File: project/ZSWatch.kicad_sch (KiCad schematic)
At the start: 35 parts, among them IC1 nPM1300-QEXX, IC2 TS3USB221A, IC3 AT25SL128A, M1 NORA-B106, X1 DOCK, X2 INT, X3 VBAT, X4 VBUS, X5 3V3

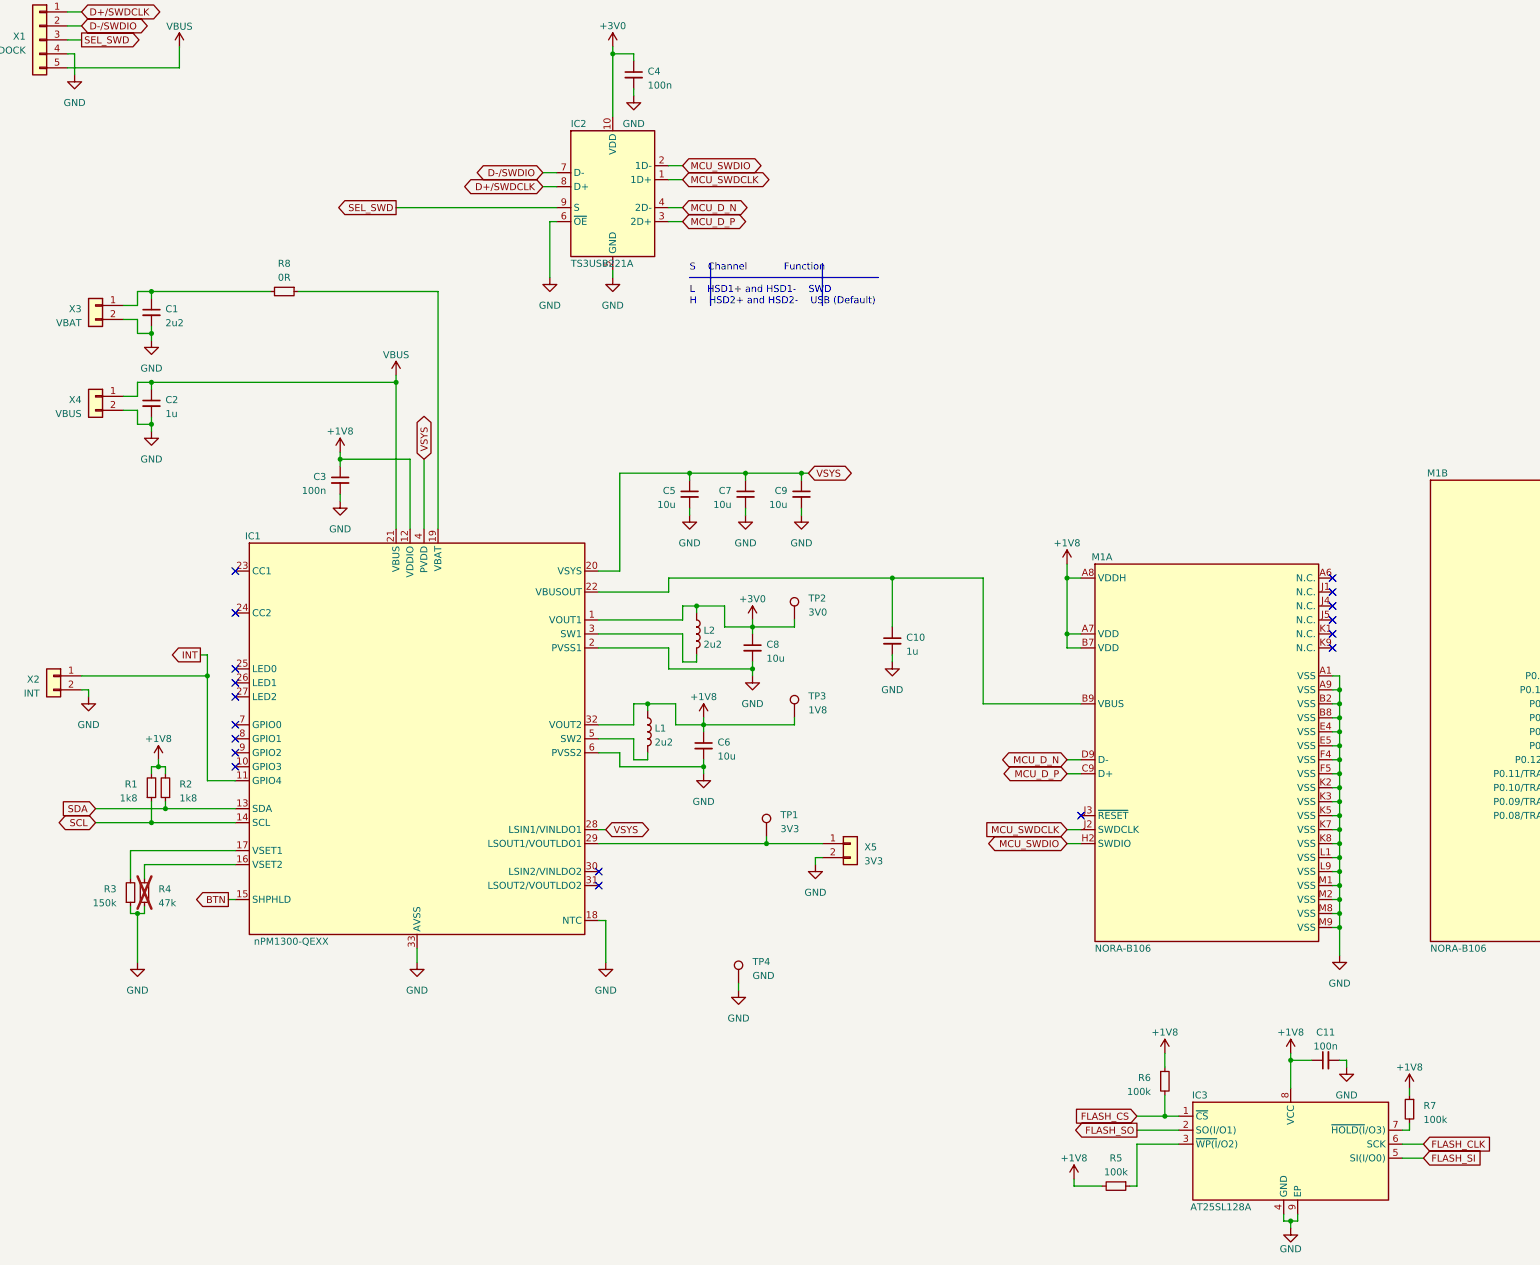
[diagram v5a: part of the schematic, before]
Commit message: Add additional jumper for SEL pin
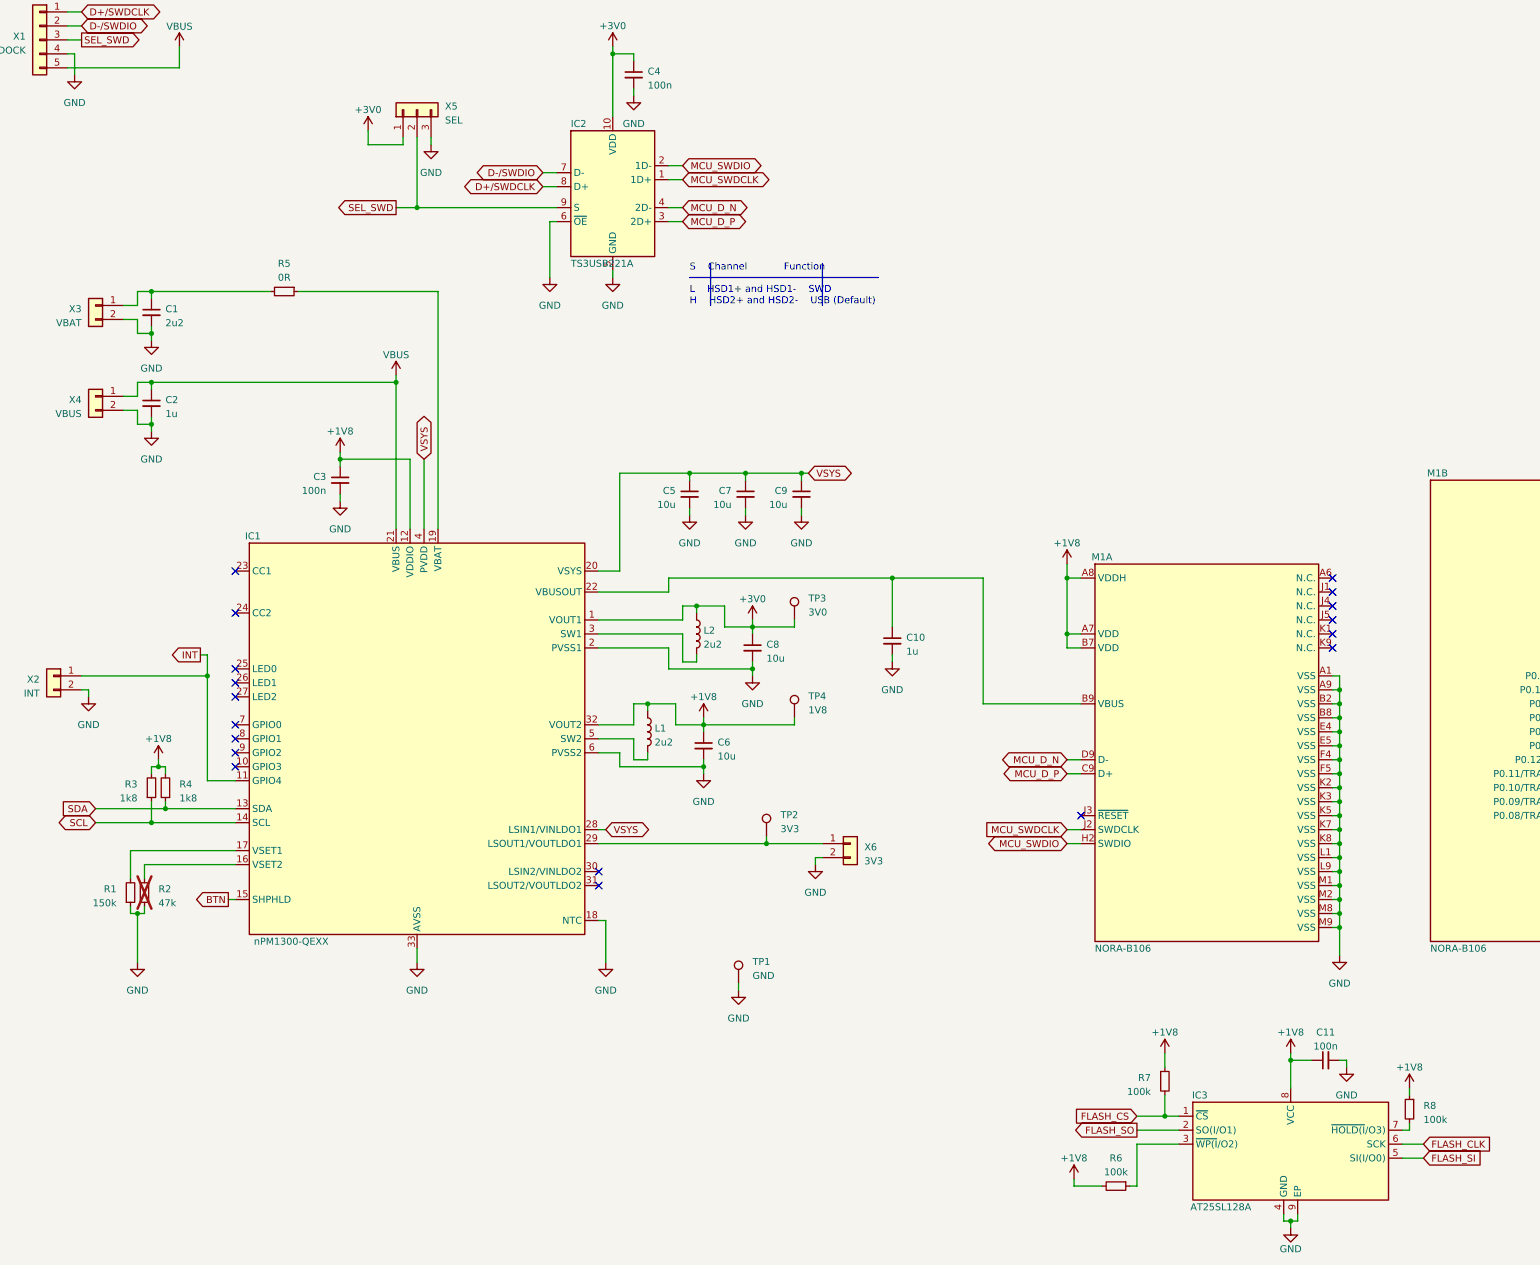
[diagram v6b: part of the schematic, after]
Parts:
- added X5: SEL, Connector_PinHeader_2.54mm:PinHeader_1x03_P2.54mm_Vertical, symbol Connector_Generic:Conn_01x03
- renumbered R3 to R1, R4 to R2, R1 to R3, R2 to R4, R8 to R5, R5 to R6, R6 to R7, R7 to R8, TP4 to TP1, TP1 to TP2, TP2 to TP3, TP3 to TP4, X5 to X6
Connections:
- net +3V0: now also X5.1 (Pin_1)
- net GND: now also X5.3 (Pin_3)
- net SEL_SWD: now also X5.2 (Pin_2)

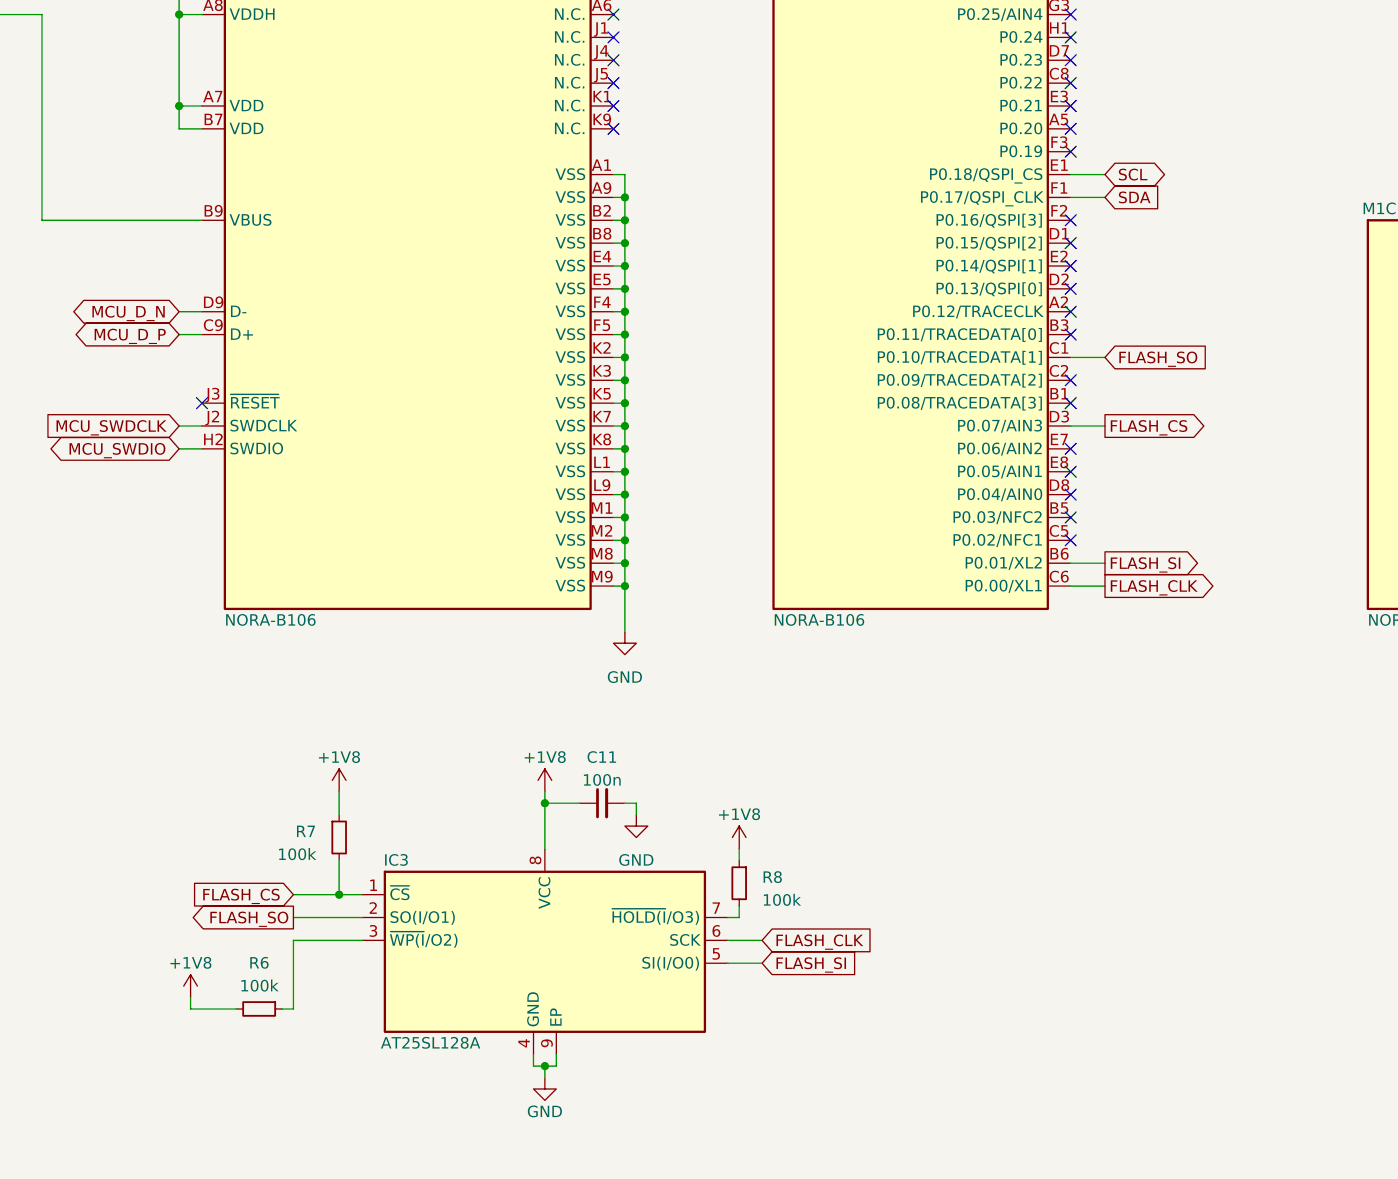
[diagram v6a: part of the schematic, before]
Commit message: Add QSPI for flash
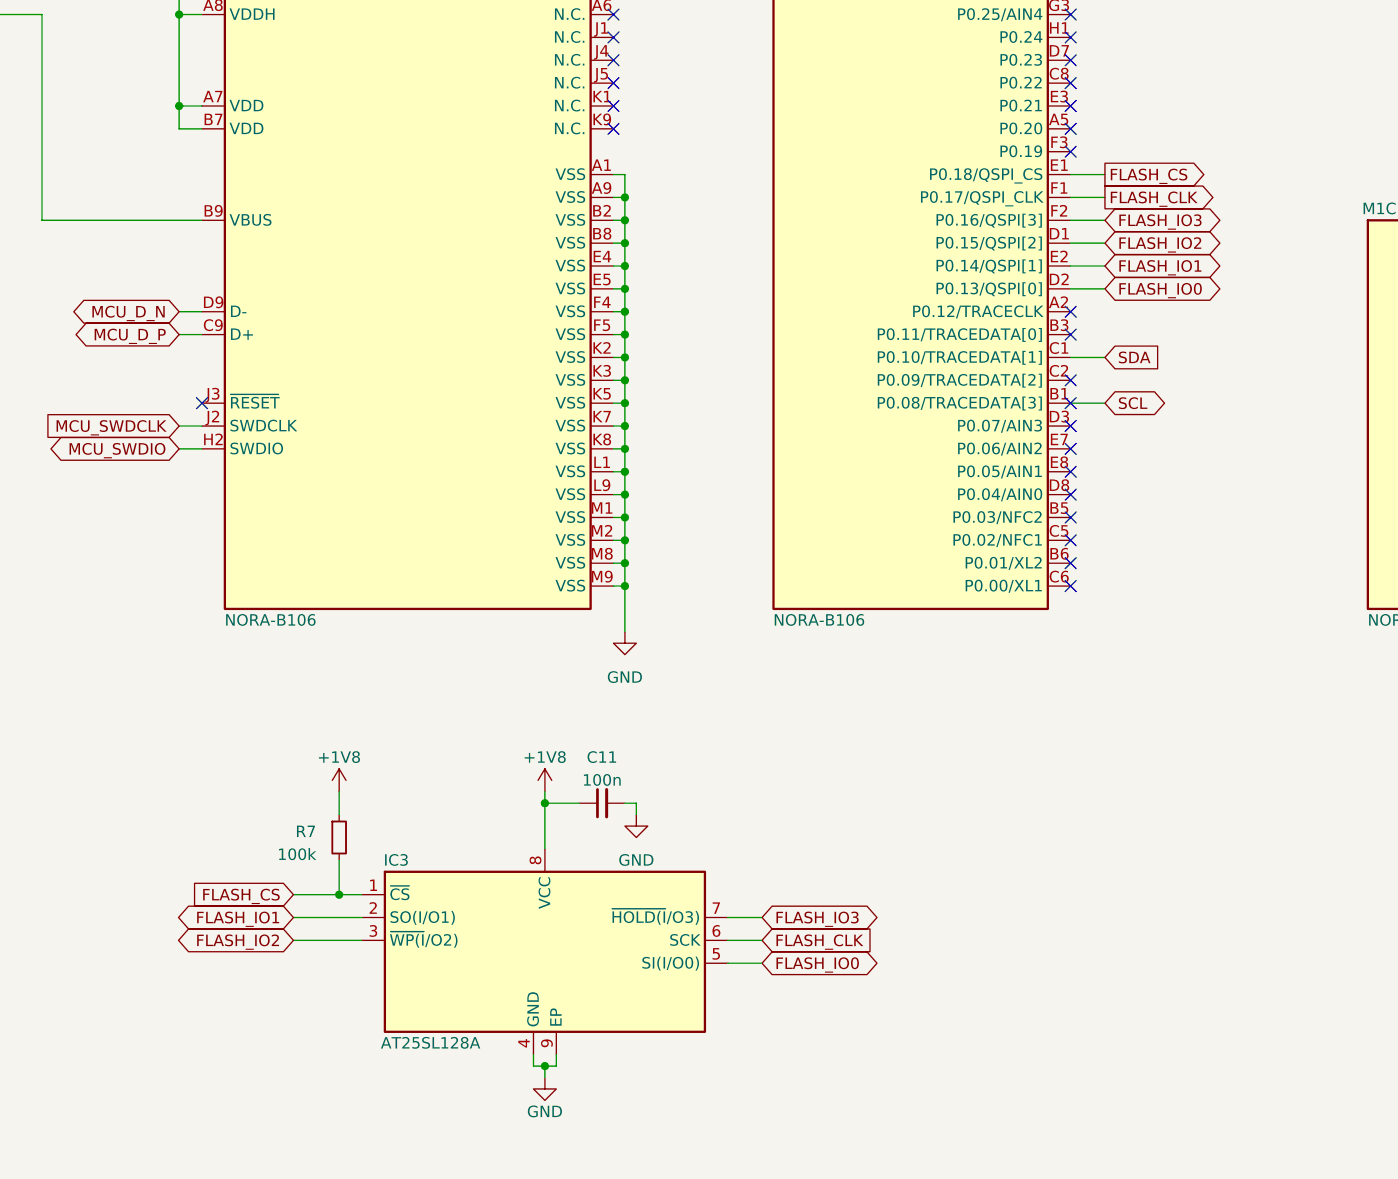
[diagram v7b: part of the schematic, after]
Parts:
- removed R6, R8: 100k, Resistor_SMD:R_0603_1608Metric, symbol Device:R_Small
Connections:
- net FLASH_CLK: now also M1.F1 (P0.17/QSPI_CLK); no longer M1.C6 (P0.00/XL1)
- net FLASH_CS: now also M1.E1 (P0.18/QSPI_CS); no longer M1.D3 (P0.07/AIN3)
- net SCL: now also M1.B1 (P0.08/TRACEDATA[3]); no longer M1.E1 (P0.18/QSPI_CS)
- net SDA: now also M1.C1 (P0.10/TRACEDATA[1]); no longer M1.F1 (P0.17/QSPI_CLK)
- net FLASH_IO2: now reaches IC3.3 (~{WP(I}/O2))
- net FLASH_IO2: now also M1.D1 (P0.15/QSPI[2])
- net FLASH_IO0: now reaches M1.D2 (P0.13/QSPI[0])
- net FLASH_IO0: now also IC3.5 (SI(I/O0))
- net FLASH_IO1: now reaches M1.E2 (P0.14/QSPI[1])
- net FLASH_IO1: now also IC3.2 (SO(I/O1))
- net FLASH_IO3: now reaches M1.F2 (P0.16/QSPI[3])
- net FLASH_IO3: now also IC3.7 (~{HOLD(I}/O3))
- net FLASH_SI: no longer names the net of M1.B6 (P0.01/XL2)
- net FLASH_SI: no longer IC3.5 (SI(I/O0))
- removed net FLASH_SO: IC3.2 (SO(I/O1)), M1.C1 (P0.10/TRACEDATA[1])
- no-connect marks 57 -> 56

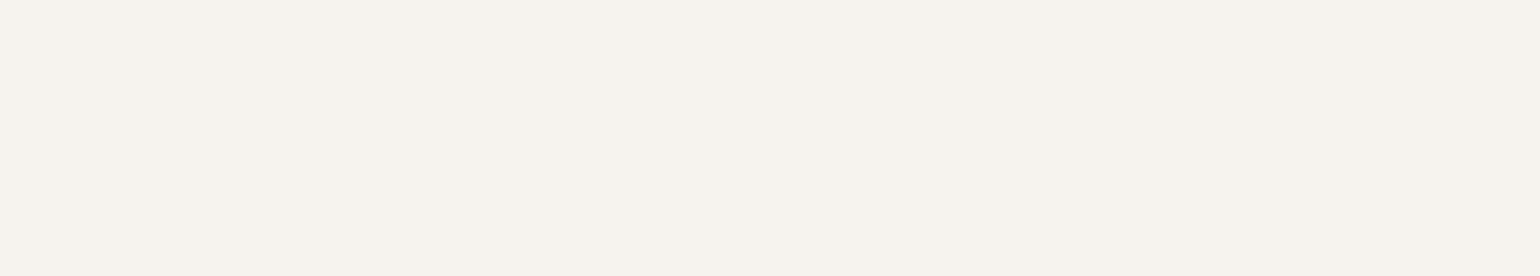
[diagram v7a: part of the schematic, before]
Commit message: Add note to schematics
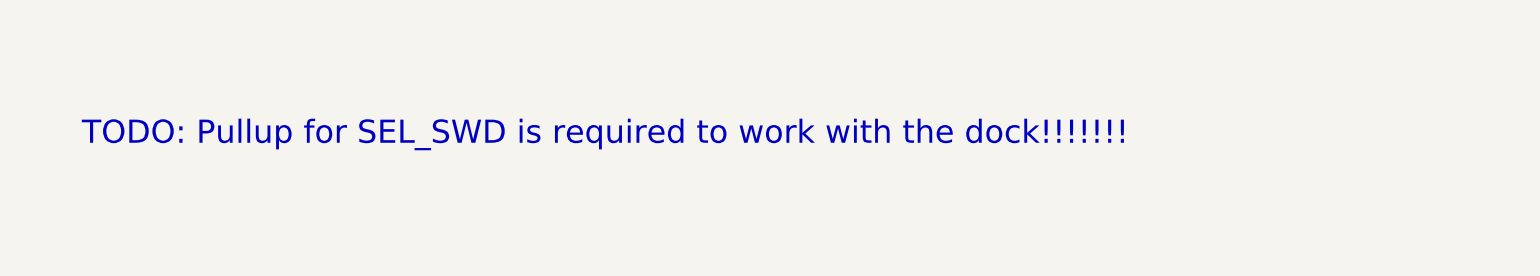
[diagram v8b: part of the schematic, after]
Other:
- note added: "TODO: Pullup for SEL_SWD is required to work with the dock!!!!!!!"
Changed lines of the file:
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@@
     (effects (font (size 1.27 1.27)) (justify left bottom))
+  )
+  (text "TODO: Pullup for SEL_SWD is required to work with the dock!!!!!!!"
+    (at 227.33 44.45 0)
+    (effects (font (size 5.08 5.08)) (justify left bottom))
   )
   (global_label "BTN" (shape output) (at 31.75 311.15 0) (fields_autoplaced)
